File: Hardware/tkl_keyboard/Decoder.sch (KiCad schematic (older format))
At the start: 10 parts, among them U7 CD74HC238, U8 CD74HC238

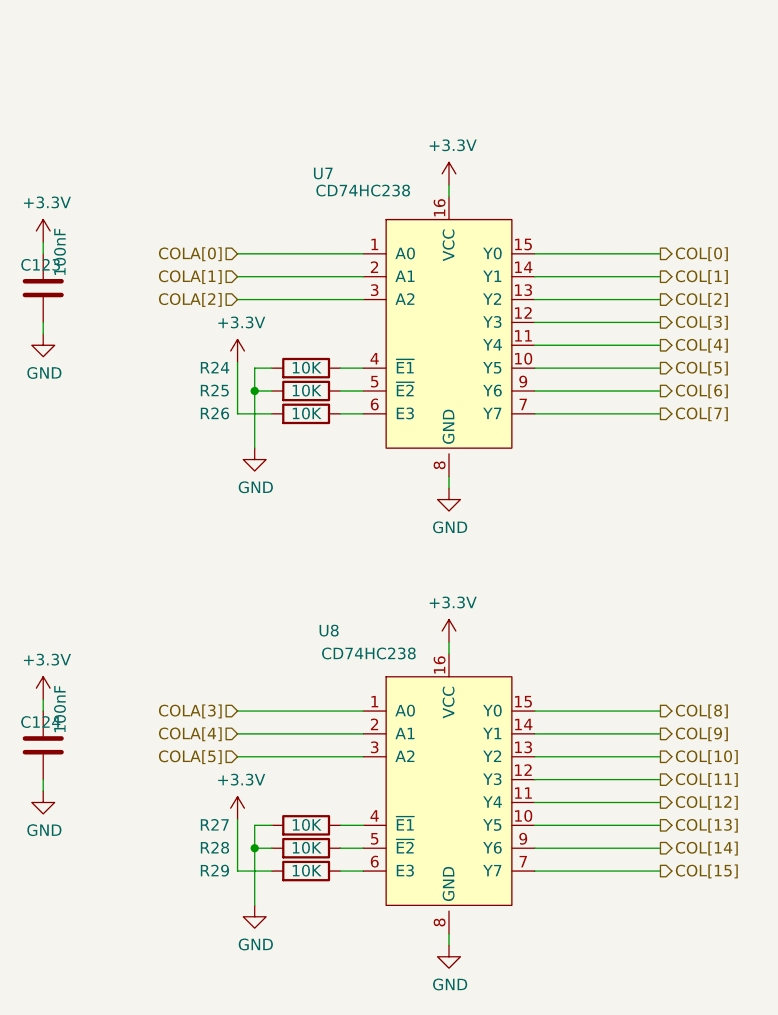
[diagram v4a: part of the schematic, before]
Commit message: Changing diode direction: row to column
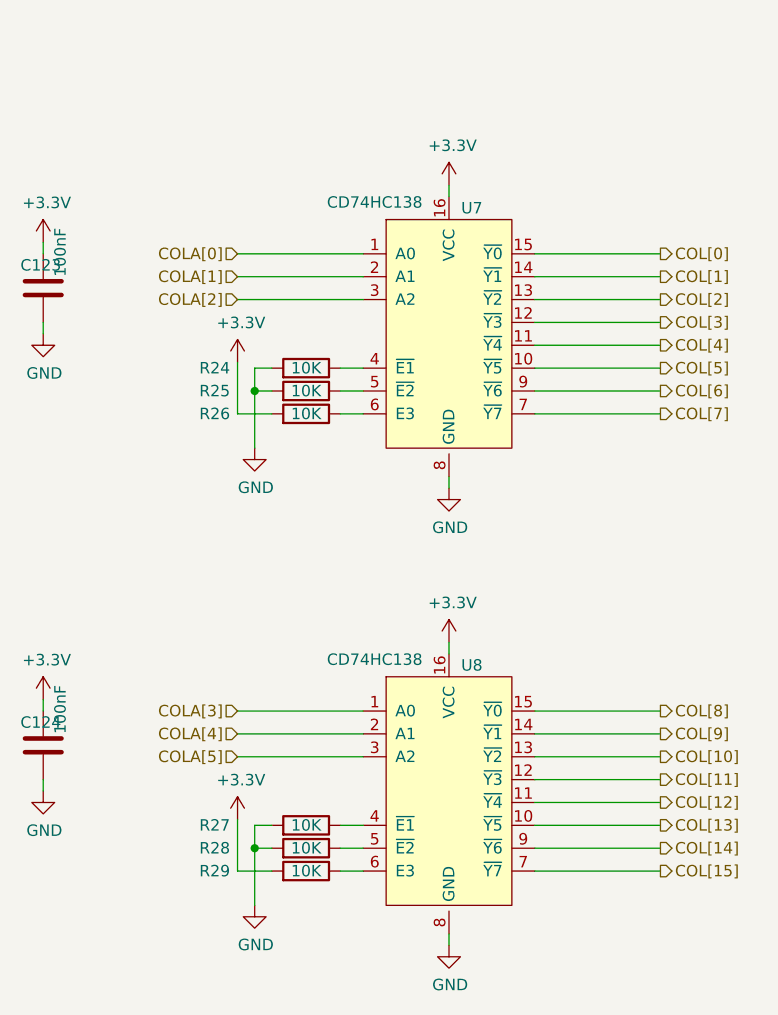
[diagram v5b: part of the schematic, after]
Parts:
- removed U7, U8: CD74HC238, Package_SO:SOIC-16_3.9x9.9mm_P1.27mm, symbol custom_parts_library:CD74HC238
- added U7, U8: CD74HC138, Package_SO:SOIC-16_3.9x9.9mm_P1.27mm, symbol custom_parts_library:CD74HC138
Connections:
- net +3V3: now also U7.16 (VCC), U8.16 (VCC)
- net COLA[0]: now also U7.1 (A0)
- net COLA[1]: now also U7.2 (A1)
- net COLA[2]: now also U7.3 (A2)
- net COLA[3]: now also U8.1 (A0)
- net COLA[4]: now also U8.2 (A1)
- net COLA[5]: now also U8.3 (A2)
- net COL[0]: now also U7.15 (~Y0~)
- net COL[10]: now also U8.13 (~Y2~)
- net COL[11]: now also U8.12 (~Y3~)
- net COL[12]: now also U8.11 (~Y4~)
- net COL[13]: now also U8.10 (~Y5~)
- net COL[14]: now also U8.9 (~Y6~)
- net COL[15]: now also U8.7 (~Y7~)
- net COL[1]: now also U7.14 (~Y1~)
- net COL[2]: now also U7.13 (~Y2~)
- net COL[3]: now also U7.12 (~Y3~)
- net COL[4]: now also U7.11 (~Y4~)
- net COL[5]: now also U7.10 (~Y5~)
- net COL[6]: now also U7.9 (~Y6~)
- net COL[7]: now also U7.7 (~Y7~)
- net COL[8]: now also U8.15 (~Y0~)
- net COL[9]: now also U8.14 (~Y1~)
- net GND: now also U7.8 (GND), U8.8 (GND)
- net at R24.1: now also U7.4 (~E1~)
- net at R25.1: now also U7.5 (~E2~)
- net at R26.1: now also U7.6 (E3)
- net at R27.1: now also U8.4 (~E1~)
- net at R28.1: now also U8.5 (~E2~)
- net at R29.1: now also U8.6 (E3)
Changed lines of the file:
@@
 Column Line Decoders
-$Comp
-L custom_parts_library:CD74HC238 U7
-U 1 1 6311A92E
-P 5775 3500
-F 0 "U7" H 5225 4700 50  0000 C CNN
-F 1 "CD74HC238" H 5400 4625 50  0000 C CNN
-F 2 "Package_SO:SOIC-16_3.9x9.9mm_P1.27mm" H 5150 4600 50  0001 C CNN
-F 3 "" H 5150 4600 50  0001 C CNN
-	1    5775 3500
-	1    0    0    -1
-$EndComp
-$Comp
-L custom_parts_library:CD74HC238 U8
-U 1 1 6311B6F2
-P 5775 5500
-F 0 "U8" H 5250 6700 50  0000 C CNN
-F 1 "CD74HC238" H 5425 6600 50  0000 C CNN
-F 2 "Package_SO:SOIC-16_3.9x9.9mm_P1.27mm" H 5150 6600 50  0001 C CNN
-F 3 "" H 5150 6600 50  0001 C CNN
-	1    5775 5500
-	1    0    0    -1
-$EndComp
 $Comp
 L power:+3.3V #PWR?
@@
 Text HLabel 4850 4650 0    50   Input ~ 0
 COLA[3]
-Wire Wire Line
-	4850 4650 5400 4650
 Text HLabel 4850 4750 0    50   Input ~ 0
 COLA[4]
-Wire Wire Line
-	4850 4750 5400 4750
 Text HLabel 4850 4850 0    50   Input ~ 0
 COLA[5]
-Wire Wire Line
-	4850 4850 5400 4850
 Text HLabel 6700 2650 2    50   Output ~ 0
 COL[0]
@@
 	0    1    -1   0
 $EndComp
-Wire Wire Line
-	5300 5250 5400 5250
-Wire Wire Line
-	5300 5350 5400 5350
-Wire Wire Line
-	5300 5150 5400 5150
 $Comp
 L power:GND #PWR?
@@
 	1    0    0    -1
 $EndComp
+$Comp
+L custom_parts_library:CD74HC138 U7
+U 1 1 614D77B4
+P 5775 3500
+F 0 "U7" H 5875 4550 50  0000 C CNN
+F 1 "CD74HC138" H 5450 4575 50  0000 C CNN
+F 2 "Package_SO:SOIC-16_3.9x9.9mm_P1.27mm" H 5225 4575 50  0001 C CNN
+F 3 "" H 5225 4575 50  0001 C CNN
+	1    5775 3500
+	1    0    0    -1
+$EndComp
+Wire Wire Line
+	5300 5350 5400 5350
+Wire Wire Line
+	5300 5250 5400 5250
+Wire Wire Line
+	5300 5150 5400 5150
+Wire Wire Line
+	4850 4850 5400 4850
+Wire Wire Line
+	4850 4750 5400 4750
+Wire Wire Line
+	4850 4650 5400 4650
+$Comp
+L custom_parts_library:CD74HC138 U8
+U 1 1 614D9BD8
+P 5775 5500
+F 0 "U8" H 5875 6550 50  0000 C CNN
+F 1 "CD74HC138" H 5450 6575 50  0000 C CNN
+F 2 "Package_SO:SOIC-16_3.9x9.9mm_P1.27mm" H 5225 6575 50  0001 C CNN
+F 3 "" H 5225 6575 50  0001 C CNN
+	1    5775 5500
+	1    0    0    -1
+$EndComp

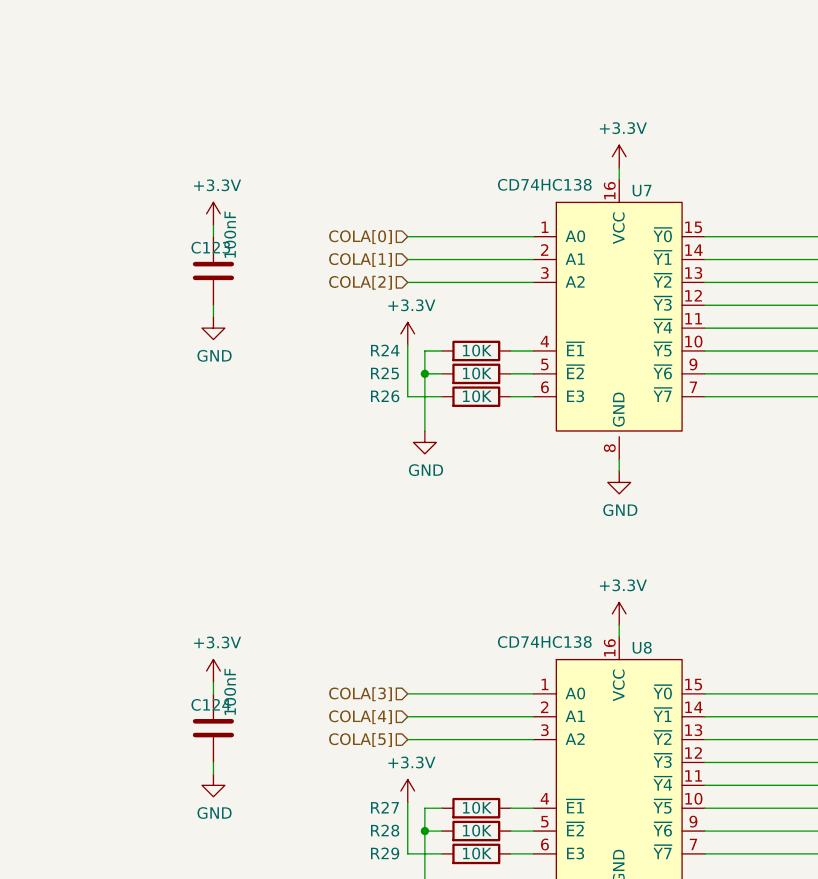
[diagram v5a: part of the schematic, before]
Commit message: Tidying schematic
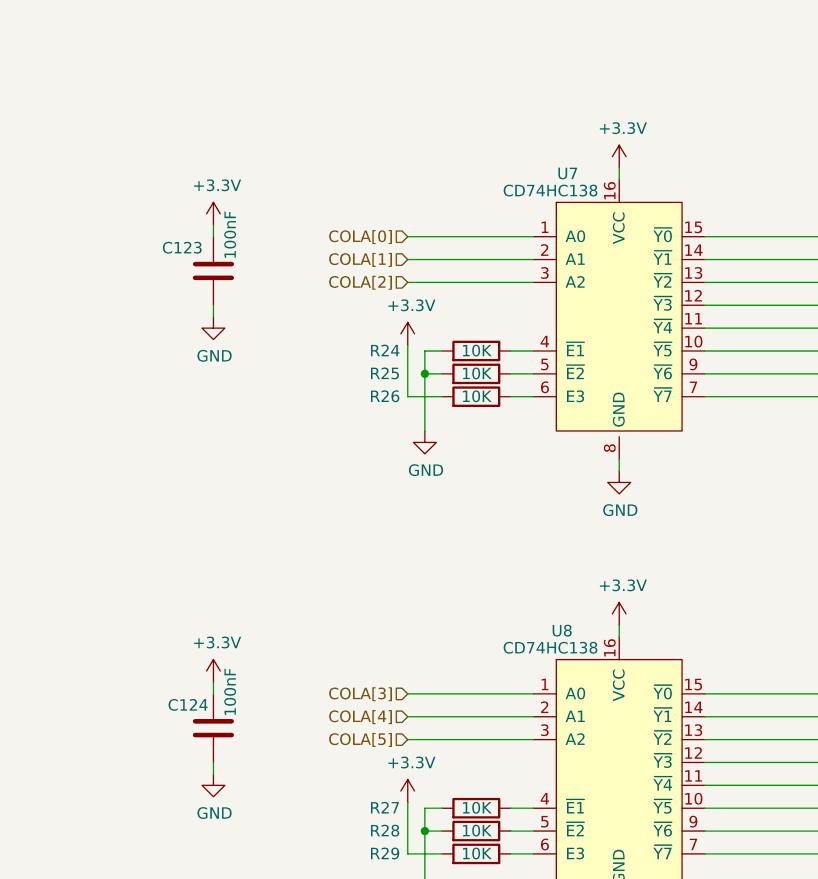
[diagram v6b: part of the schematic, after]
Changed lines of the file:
@@
 encoding utf-8
 Sheet 6 12
-Title ""
+Title "TKL Keyboard"
 Date ""
-Rev ""
+Rev "0"
 Comp ""
 Comment1 ""
@@
 AR Path="/62FB59AD/616D26C3" Ref="C?"  Part="1"
 AR Path="/6301FD9D/616D26C3" Ref="C123"  Part="1"
-F 0 "C123" H 3900 2900 50  0000 L CNN
+F 0 "C123" H 3775 2900 50  0000 L CNN
 F 1 "100nF" V 4075 2850 50  0000 L CNN
 F 2 "Capacitor_smd:C_0603_1608Metric" H 4038 2650 50  0001 C CNN
@@
 AR Path="/62FB59AD/616D9D8E" Ref="C?"  Part="1"
 AR Path="/6301FD9D/616D9D8E" Ref="C124"  Part="1"
-F 0 "C124" H 3900 4900 50  0000 L CNN
+F 0 "C124" H 3800 4900 50  0000 L CNN
 F 1 "100nF" V 4075 4850 50  0000 L CNN
 F 2 "Capacitor_smd:C_0603_1608Metric" H 4038 4650 50  0001 C CNN
@@
 U 1 1 614D77B4
 P 5775 3500
-F 0 "U7" H 5875 4550 50  0000 C CNN
-F 1 "CD74HC138" H 5450 4575 50  0000 C CNN
+F 0 "U7" H 5550 4625 50  0000 C CNN
+F 1 "CD74HC138" H 5475 4550 50  0000 C CNN
 F 2 "Package_SO:SOIC-16_3.9x9.9mm_P1.27mm" H 5225 4575 50  0001 C CNN
 F 3 "" H 5225 4575 50  0001 C CNN
@@
 U 1 1 614D9BD8
 P 5775 5500
-F 0 "U8" H 5875 6550 50  0000 C CNN
-F 1 "CD74HC138" H 5450 6575 50  0000 C CNN
+F 0 "U8" H 5525 6625 50  0000 C CNN
+F 1 "CD74HC138" H 5475 6550 50  0000 C CNN
 F 2 "Package_SO:SOIC-16_3.9x9.9mm_P1.27mm" H 5225 6575 50  0001 C CNN
 F 3 "" H 5225 6575 50  0001 C CNN
